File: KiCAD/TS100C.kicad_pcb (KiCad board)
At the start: 4 copper layers, 84 x 10 mm, 63 parts, among them J1 USB_C_Receptacle_USB2.0, J2 OLED_64x32, J3 A, J4 B, J5 DNP, P1 TC2030-CTX, Q1 SS8050, Q2 DMP3017SFG, SW1 key1, SW2 key2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

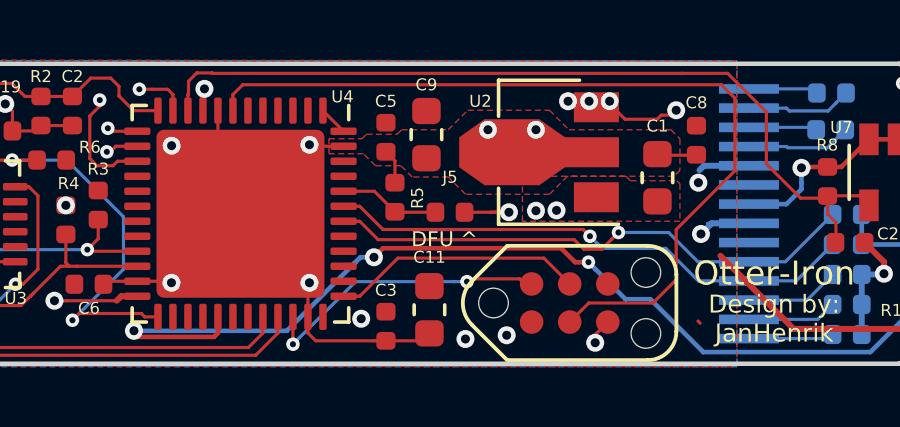
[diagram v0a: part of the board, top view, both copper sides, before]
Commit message: Hook up SW1 to BOOT0 too
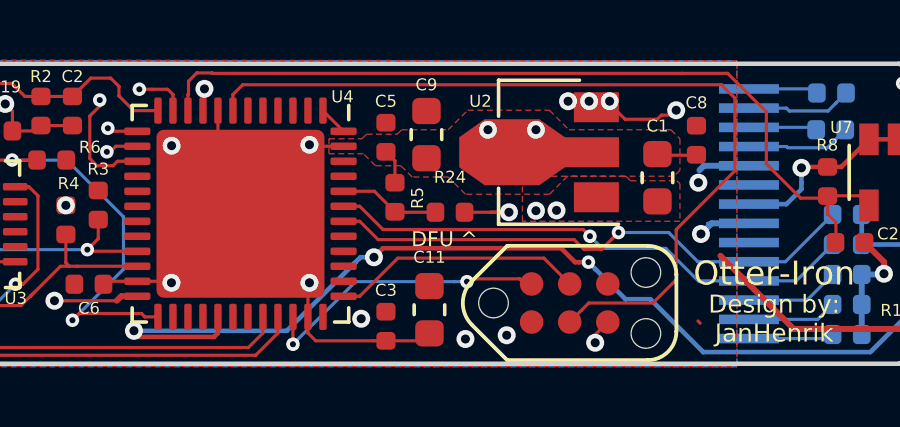
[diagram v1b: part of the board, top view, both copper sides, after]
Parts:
- R24: renamed from J5; value DNP -> 2k3
- R5: value 2k37 -> 10k
- U3: value STUSB4500 -> STUSB4500QTR
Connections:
- R24 pad 2: +3V3 -> BOOT0
- SW1 pad 2: Net-(SW1-Pad2) -> BOOT0
- U4 pad 13: Net-(SW1-Pad2) -> BOOT0
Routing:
- net BOOT0: track 0.00 -> 50.0 mm, vias 0 -> 3
- net Net-(SW1-Pad2): track 43.2 -> 0.00 mm, vias 2 -> 0
- net +3V3: track 77.1 -> 75.0 mm, vias 19 -> 18
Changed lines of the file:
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@@
-(kicad_pcb (version 20171130) (host pcbnew 5.1.4+dfsg1-1)
+(kicad_pcb (version 20171130) (host pcbnew 5.1.5-52549c5~84~ubuntu19.04.1)
   (general
     (thickness 1.6)
     (drawings 12)
-    (tracks 631)
+    (tracks 635)
     (zones 0)
     (modules 63)
@@
   )
   (setup
-    (last_trace_width 0.2)
+    (last_trace_width 0.106)
     (user_trace_width 0.106)
     (user_trace_width 0.154)
@@
   (net 76 "Net-(U4-Pad45)")
   (net 77 "Net-(U4-Pad39)")
-  (net 78 "Net-(J5-Pad1)")
-  (net 79 "Net-(SW1-Pad2)")
+  (net 78 "Net-(R24-Pad1)")
+  (net 79 BOOT0)
   (net_class Default "This is the default net class."
     (clearance 0.154)
@@
     (add_net +3V3)
     (add_net /OUT)
+    (add_net BOOT0)
     (add_net CC1)
     (add_net CC2)
@@
     (add_net "Net-(J2-Pad6)")
     (add_net "Net-(J2-Pad9)")
-    (add_net "Net-(J5-Pad1)")
     (add_net "Net-(P1-Pad6)")
     (add_net "Net-(Q1-Pad1)")
@@
     (add_net "Net-(R21-Pad1)")
     (add_net "Net-(R23-Pad1)")
+    (add_net "Net-(R24-Pad1)")
     (add_net "Net-(R7-Pad2)")
-    (add_net "Net-(SW1-Pad2)")
     (add_net "Net-(SW2-Pad2)")
     (add_net "Net-(U3-Pad11)")
@@
     (tags resistor)
     (attr smd)
-    (fp_text reference J5 (at 0 -1.17) (layer F.SilkS)
+    (fp_text reference R24 (at 0 -1.17) (layer F.SilkS)
       (effects (font (size 0.4 0.4) (thickness 0.1)))
     )
-    (fp_text value DNP (at 0 1.17) (layer F.Fab)
+    (fp_text value 2k3 (at 0 1.17) (layer F.Fab)
       (effects (font (size 1 1) (thickness 0.15)))
     )
@@
     (fp_line (start -0.5 0.25) (end -0.5 -0.25) (layer F.Fab) (width 0.1))
     (pad 2 smd roundrect (at 0.485 0) (size 0.59 0.64) (layers F.Cu F.Paste F.Mask) (roundrect_rratio 0.25)
-      (net 9 +3V3))
+      (net 79 BOOT0))
     (pad 1 smd roundrect (at -0.485 0) (size 0.59 0.64) (layers F.Cu F.Paste F.Mask) (roundrect_rratio 0.25)
-      (net 78 "Net-(J5-Pad1)"))
+      (net 78 "Net-(R24-Pad1)"))
     (model ${KISYS3DMOD}/Resistor_SMD.3dshapes/R_0402_1005Metric.wrl
       (at (xyz 0 0 0))
@@
       (effects (font (size 0.4 0.4) (thickness 0.1)))
     )
-    (fp_text value STUSB4500 (at 0 3.32) (layer F.Fab)
+    (fp_text value STUSB4500QTR (at 0 3.32) (layer F.Fab)
       (effects (font (size 1 1) (thickness 0.15)))
     )
@@
       (net 9 +3V3))
     (pad 2 smd rect (at -2.075 -1.075 90) (size 1.05 0.65) (layers B.Cu B.Paste B.Mask)
-      (net 79 "Net-(SW1-Pad2)"))
+      (net 79 BOOT0))
     (pad 2 smd rect (at 2.075 -1.075 90) (size 1.05 0.65) (layers B.Cu B.Paste B.Mask)
-      (net 79 "Net-(SW1-Pad2)"))
+      (net 79 BOOT0))
     (model ${KISYS3DMOD}/Button_Switch_SMD.3dshapes/SW_SPST_PTS810.wrl
       (at (xyz 0 0 0))
@@
       (net 76 "Net-(U4-Pad45)"))
     (pad 44 smd roundrect (at -0.75 -3.4375 270) (size 0.25 0.875) (layers F.Cu F.Paste F.Mask) (roundrect_rratio 0.25)
-      (net 78 "Net-(J5-Pad1)"))
+      (net 78 "Net-(R24-Pad1)"))
     (pad 43 smd roundrect (at -0.25 -3.4375 270) (size 0.25 0.875) (layers F.Cu F.Paste F.Mask) (roundrect_rratio 0.25)
       (net 2 OLED_SDA))
@@
       (net 51 "Net-(SW2-Pad2)"))
     (pad 13 smd roundrect (at -2.75 3.4375 270) (size 0.25 0.875) (layers F.Cu F.Paste F.Mask) (roundrect_rratio 0.25)
-      (net 79 "Net-(SW1-Pad2)"))
+      (net 79 BOOT0))
     (pad 12 smd roundrect (at -3.4375 2.75 270) (size 0.875 0.25) (layers F.Cu F.Paste F.Mask) (roundrect_rratio 0.25)
       (net 44 UIN))
@@
       (effects (font (size 0.4 0.4) (thickness 0.1)))
     )
-    (fp_text value 2k37 (at 0 1.17 90) (layer F.Fab)
+    (fp_text value 10k (at 0 1.17 90) (layer F.Fab)
       (effects (font (size 1 1) (thickness 0.15)))
     )
@@
     (fp_line (start -0.5 0.25) (end -0.5 -0.25) (layer F.Fab) (width 0.1))
     (pad 2 smd roundrect (at 0.485 0 270) (size 0.59 0.64) (layers F.Cu F.Paste F.Mask) (roundrect_rratio 0.25)
-      (net 78 "Net-(J5-Pad1)"))
+      (net 78 "Net-(R24-Pad1)"))
     (pad 1 smd roundrect (at -0.485 0 270) (size 0.59 0.64) (layers F.Cu F.Paste F.Mask) (roundrect_rratio 0.25)
       (net 1 GND))
@@
   (via (at 123.314163 83.964163) (size 0.6) (drill 0.3) (layers F.Cu B.Cu) (net 9))
   (via (at 123.4 85.675) (size 0.6) (drill 0.3) (layers F.Cu B.Cu) (net 9))
-  (segment (start 116.37 84.95) (end 117 84.95) (width 0.106) (layer F.Cu) (net 9))
-  (via (at 117 84.95) (size 0.6) (drill 0.3) (layers F.Cu B.Cu) (net 9))
+  (segment (start 116.37 84.95) (end 117 84.95) (width 0.106) (layer F.Cu) (net 79))
+  (via (at 117 84.95) (size 0.6) (drill 0.3) (layers F.Cu B.Cu) (net 79))
   (segment (start 111.4875 82.25) (end 110.8 81.5625) (width 0.106) (layer F.Cu) (net 9))
   (segment (start 92.87 82.63) (end 92.905 82.595) (width 0.106) (layer F.Cu) (net 9))
@@
   (segment (start 131.55 88.45) (end 131.15 88.85) (width 0.154) (layer B.Cu) (net 9))
   (segment (start 130.575 86.025) (end 131.55 87) (width 0.154) (layer B.Cu) (net 9))
-  (segment (start 115.52 84.95) (end 117 84.95) (width 0.106) (layer F.Cu) (net 9))
+  (segment (start 115.52 84.95) (end 117 84.95) (width 0.106) (layer F.Cu) (net 79))
   (via (at 101.849996 87.9) (size 0.6) (drill 0.3) (layers F.Cu B.Cu) (net 9))
   (segment (start 102.27426 87.9) (end 101.849996 87.9) (width 0.106) (layer F.Cu) (net 9))
@@
   (segment (start 107.29 81.4) (end 108.09 80.6) (width 0.106) (layer In2.Cu) (net 79))
   (segment (start 129.554786 81.35) (end 131.914024 81.35) (width 0.106) (layer In2.Cu) (net 79))
-  (segment (start 108.09 80.6) (end 128.804786 80.6) (width 0.106) (layer In2.Cu) (net 79))
   (segment (start 128.804786 80.6) (end 129.554786 81.35) (width 0.106) (layer In2.Cu) (net 79))
+  (segment (start 116.4 80.6) (end 116.6 80.6) (width 0.106) (layer In2.Cu) (net 79))
+  (segment (start 116.4 80.6) (end 128.804786 80.6) (width 0.106) (layer In2.Cu) (net 79))
+  (segment (start 108.09 80.6) (end 116.4 80.6) (width 0.106) (layer In2.Cu) (net 79))
+  (segment (start 117 81) (end 117 84.95) (width 0.106) (layer In2.Cu) (net 79))
+  (segment (start 116.6 80.6) (end 117 81) (width 0.106) (layer In2.Cu) (net 79))
   (zone (net 1) (net_name GND) (layer In2.Cu) (hatch edge 0.508)
     (connect_pads (clearance 0.154))
